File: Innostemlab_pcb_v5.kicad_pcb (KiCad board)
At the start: 4 copper layers, 60 x 52 mm, 32 parts, among them J10 I2C, J11 ICSP, J2 USB4105-GF-A-060, J3 BATTERY, J4 MOTOR_1, J5 MOTOR_2, J6 IR1, J7 IR2, J8 IR3, J9 Conn_02x12_Odd_Even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

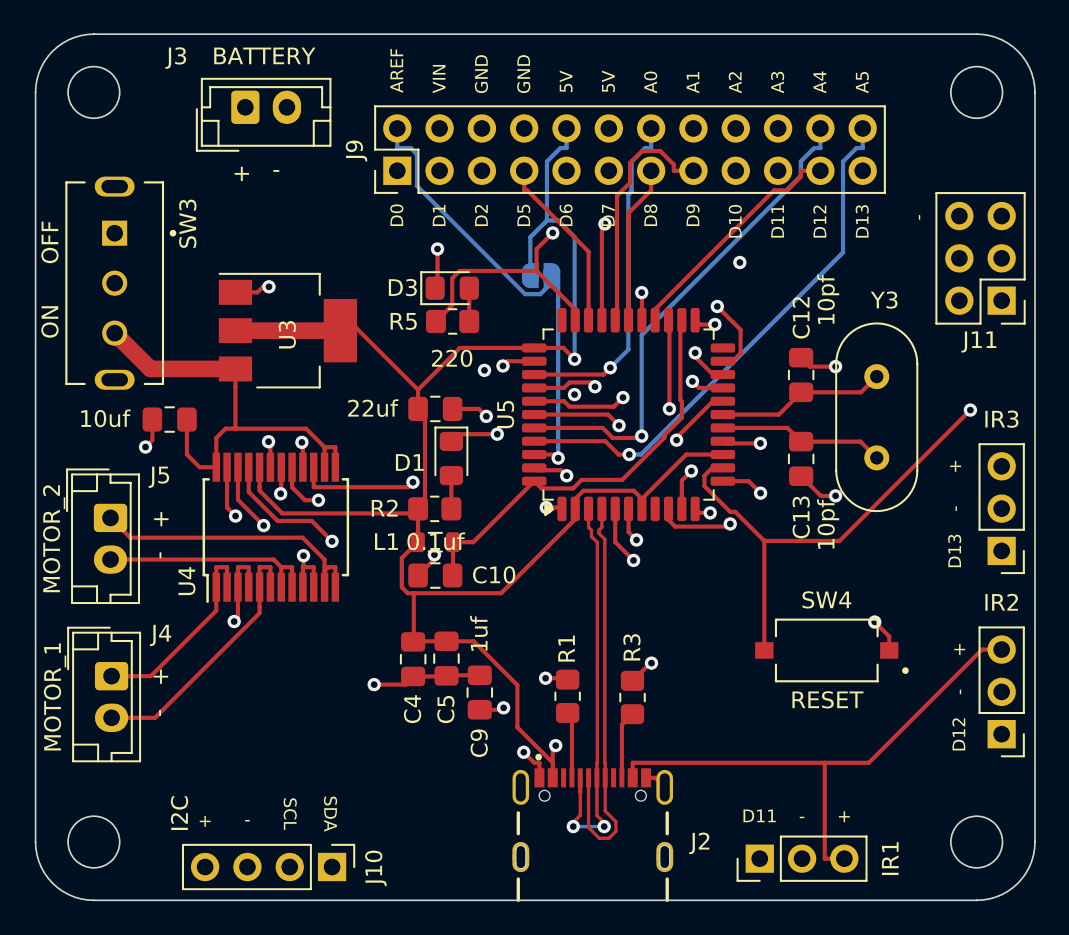
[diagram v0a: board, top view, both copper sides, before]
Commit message: Added caps in TB motor driver, added 22 ohm resistors in usb c data lines, changed part number for AVCC low pass filter, LD1117 datasheet from digikey shows same implementation
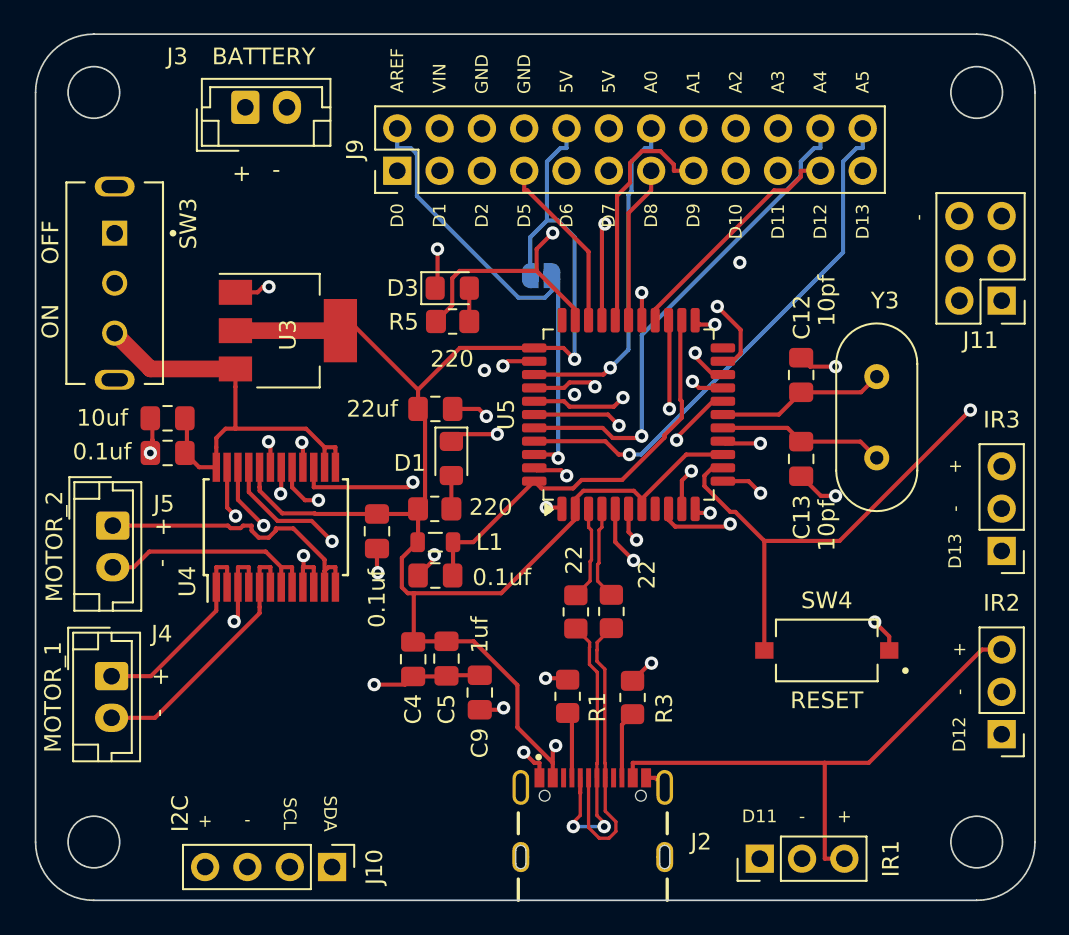
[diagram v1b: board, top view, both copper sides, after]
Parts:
- added C1: 0.1uf, Capacitor_SMD:C_0805_2012Metric_Pad1.18x1.45mm_HandSolder, F.Cu at (126.9, 109.1)
- added C2: 0.1uf, Capacitor_SMD:C_0805_2012Metric_Pad1.18x1.45mm_HandSolder, F.Cu at (139.5, 113.8)
- added R4: 22, Resistor_SMD:R_0805_2012Metric_Pad1.20x1.40mm_HandSolder, F.Cu at (153.6, 118.7)
- added R6: 22, Resistor_SMD:R_0805_2012Metric_Pad1.20x1.40mm_HandSolder, F.Cu at (151.4, 118.7)
- moved J5 0.48 mm to (123.6, 113.5)
- moved C7 0.15 mm to (126.9, 107.1)
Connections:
- U5 pad 3: D- -> /DNET-
- U5 pad 4: D+ -> /DNET+
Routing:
- net D-: track 25.8 -> 18.9 mm
- net D+: track 24.9 -> 18.1 mm
- net /DNET-: track 0.00 -> 5.65 mm
- net /DNET+: track 0.00 -> 5.61 mm
- net GND: track 54.9 -> 56.6 mm, vias 21 -> 22
- net M2P: track 17.5 -> 18.3 mm
- net AREF: track 28.5 -> 29.4 mm

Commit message: changed label to left and right for motor, the other edits happened in previous commmit
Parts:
- J4: value MOTOR_1 -> LEFT M
- J5: value MOTOR_2 -> RIGHT M
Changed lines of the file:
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@@
 			)
 		)
-		(property "Value" "MOTOR_2"
+		(property "Value" "RIGHT M"
 			(at 1.25 3.5 90)
 			(layer "F.SilkS")
@@
 			)
 		)
-		(property "Value" "MOTOR_1"
+		(property "Value" "LEFT M"
 			(at 1.25 3.51 90)
 			(layer "F.SilkS")

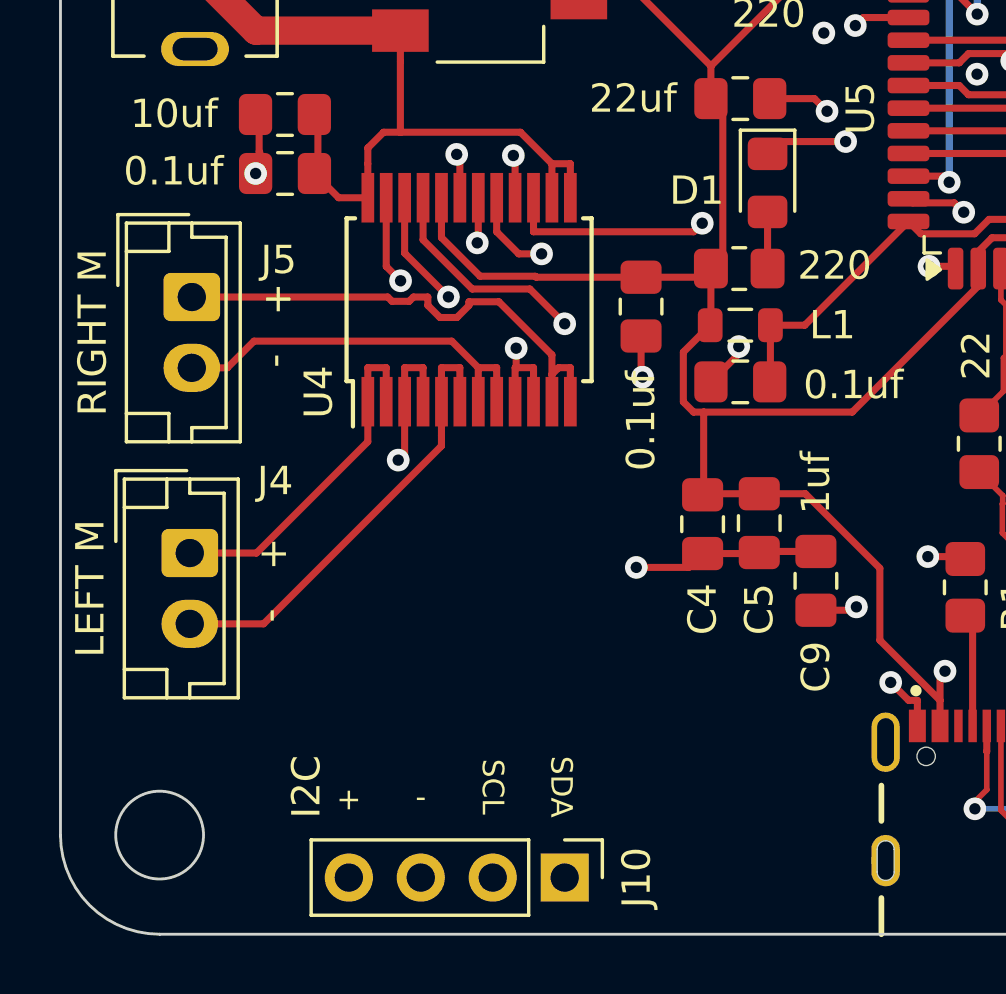
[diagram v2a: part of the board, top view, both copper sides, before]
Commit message: Added electrolytic cap, changed motor nammmes to left and right
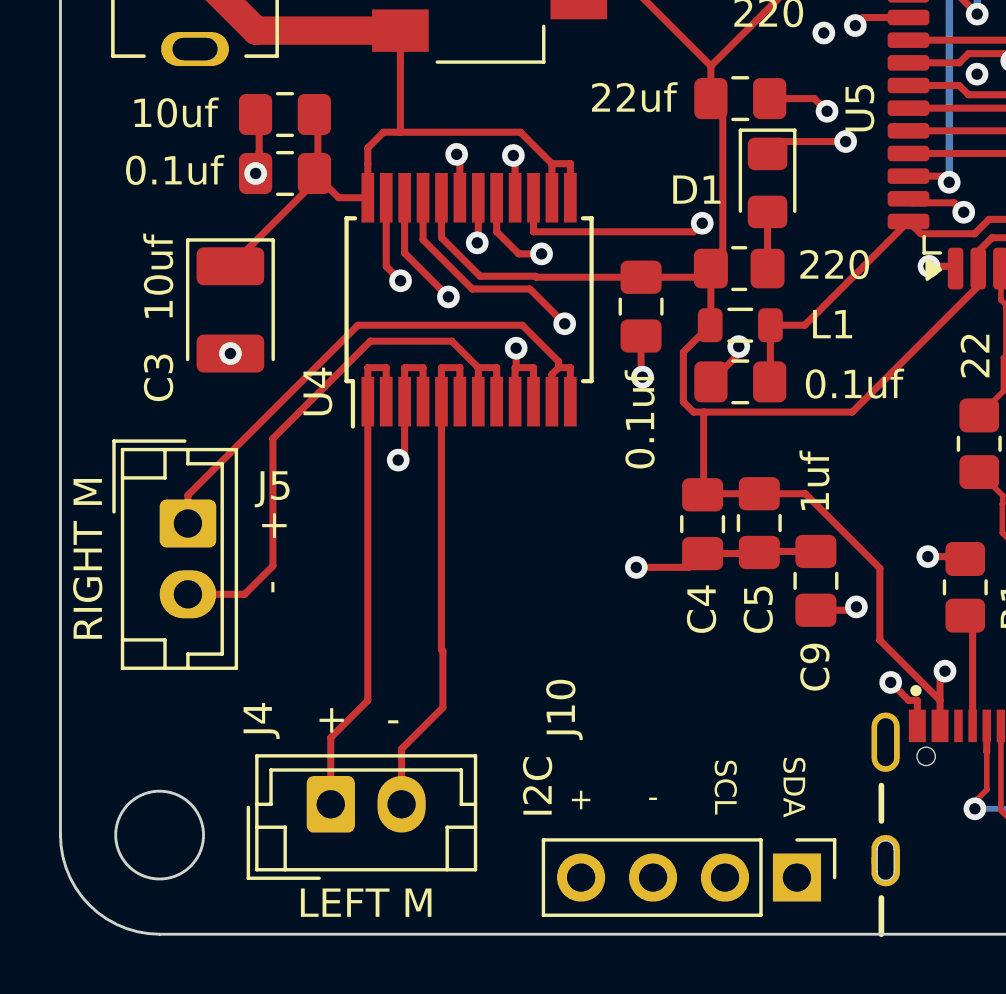
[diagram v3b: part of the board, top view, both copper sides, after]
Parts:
- added C3: 10uf, Capacitor_Tantalum_SMD:CP_EIA-3528-12_Kemet-T, F.Cu at (125.0, 114.0)
- moved J4 10.2 mm to (128.5, 131.4), turned to 0 degrees
- moved J10 8.20 mm to (145.0, 134.0)
- moved J5 8.00 mm to (123.5, 121.5)
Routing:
- net VBUS: track 231.7 -> 224.4 mm
- net M2N: track 13.9 -> 20.0 mm
- net M1P: track 12.4 -> 17.8 mm
- net VBATP_MD: track 28.0 -> 32.6 mm
- net D3: track 58.1 -> 61.5 mm
- net D2: track 68.3 -> 71.7 mm
- net M2P: track 18.3 -> 20.2 mm
- net M1N: track 16.1 -> 17.9 mm
- net GND: vias 22 -> 23

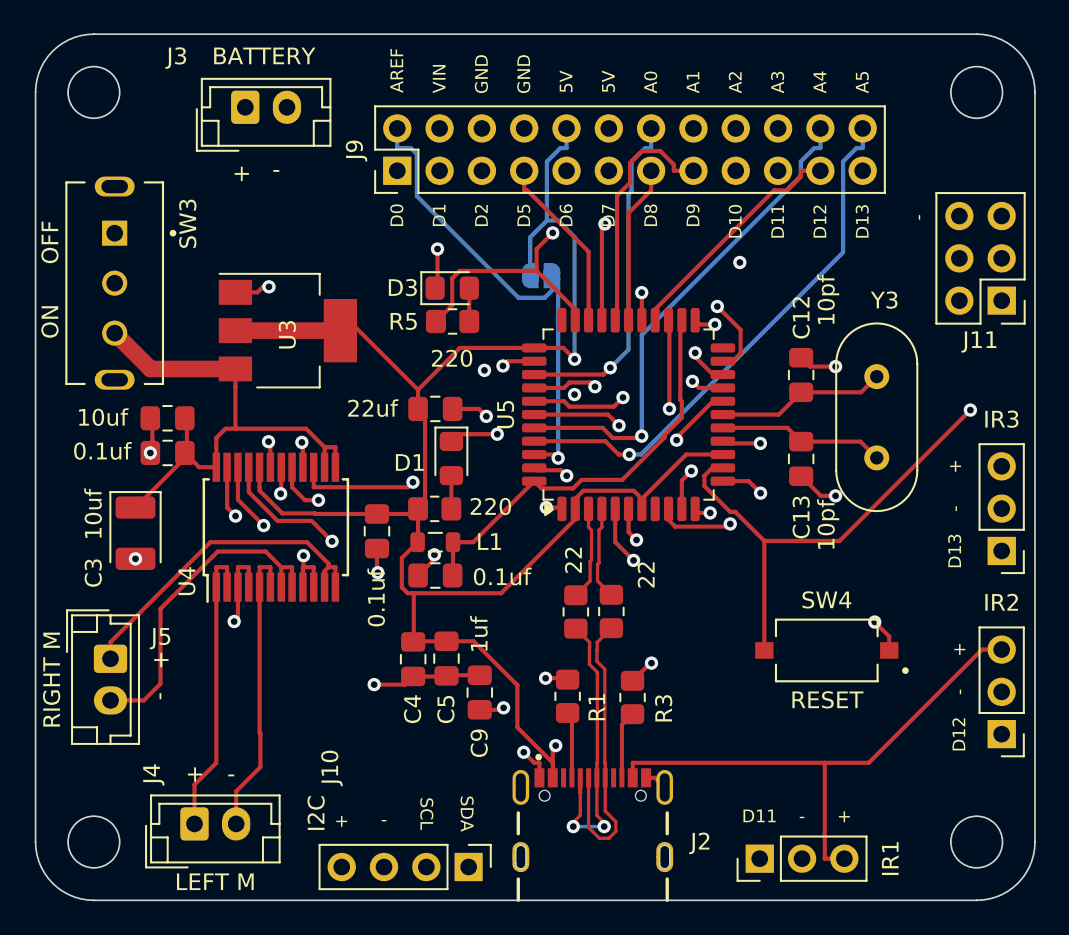
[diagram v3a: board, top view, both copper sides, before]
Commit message: updated vbus and 5v to be seperate so that usb only powers atmega chip. battery required for other sensors and components
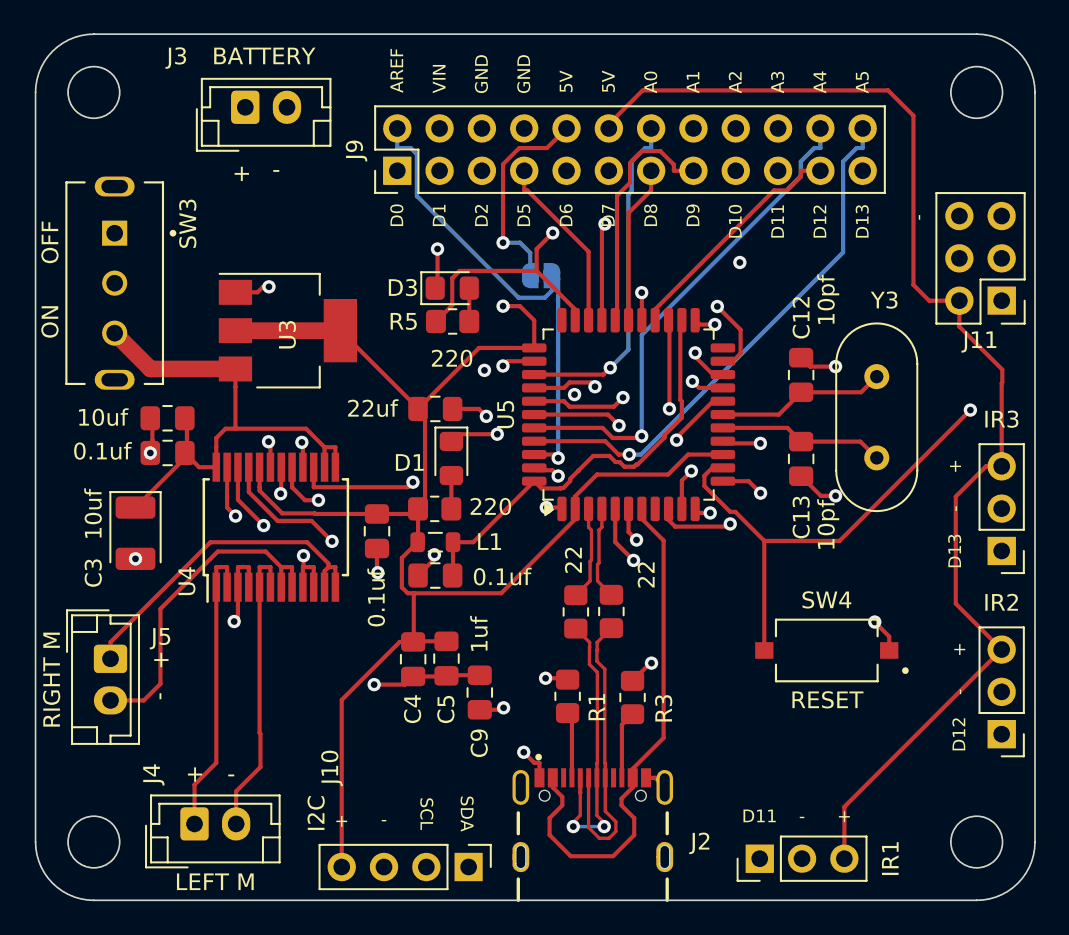
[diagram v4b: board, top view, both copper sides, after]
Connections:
- AREF2 pad 2: VBUS -> +5V
- C2 pad 2: VBUS -> +5V
- C4 pad 2: VBUS -> +5V
- C5 pad 2: VBUS -> +5V
- C8 pad 1: VBUS -> +5V
- J10 pad 4: VBUS -> +5V
- J11 pad 2: VBUS -> +5V
- J6 pad 3: VBUS -> +5V
- J7 pad 3: VBUS -> +5V
- J8 pad 3: VBUS -> +5V
- J9 pad 10: VBUS -> +5V
- J9 pad 12: VBUS -> +5V
- L1 pad 1: VBUS -> +5V
- R2 pad 1: VBUS -> +5V
- U3 pad 2: VBUS -> +5V
- U4 pad 20: VBUS -> +5V
- U5 pad 14: VBUS -> +5V
- U5 pad 2: VBUS -> +5V
- U5 pad 34: VBUS -> +5V
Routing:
- net VBUS: track 224.4 -> 31.7 mm, vias 2 -> 0
- net +5V: track 0.00 -> 187.6 mm, vias 0 -> 2
- net AVCC: track 25.2 -> 25.9 mm
- net GND: track 56.6 -> 56.1 mm
